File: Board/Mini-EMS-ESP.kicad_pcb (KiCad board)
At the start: 4 copper layers, 57.8 x 39 mm, 66 parts, among them J8 EMS, Q1 BC858, Q11 BC848, Q2 UMH3N, U1 ESP32-WROOM-32, U2 LM393, U3 MP1584, U4 CH340C, U5 USBLC6

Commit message: Minor fixes
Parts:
- C11: value 22u -> 47u
- R13, R15, R16: value 10K -> 100K
- R21: value 470 -> 220
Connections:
- net Net-(U3-EN) renamed /EMS interface/BUCK_EN
- net Net-(U3-FREQ) renamed /EMS interface/BUCK_FREQ
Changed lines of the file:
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@@
 	(net 28 "Net-(R10-Pad1)")
 	(net 29 "RX")
-	(net 30 "Net-(U3-FREQ)")
-	(net 31 "Net-(U3-EN)")
+	(net 30 "/EMS interface/BUCK_FREQ")
+	(net 31 "/EMS interface/BUCK_EN")
 	(net 32 "/EMS interface/BUCK_FB")
 	(net 33 "/CC2")
@@
 			)
 		)
-		(property "Value" "10K"
+		(property "Value" "100K"
 			(at 0 1.65 90)
 			(layer "F.Fab")
@@
 			(layers "F.Cu" "F.Mask" "F.Paste")
 			(roundrect_rratio 0.243902)
-			(net 30 "Net-(U3-FREQ)")
+			(net 30 "/EMS interface/BUCK_FREQ")
 			(pintype "passive")
 		)
@@
 			)
 		)
-		(property "Value" "10K"
+		(property "Value" "100K"
 			(at 0 1.65 0)
 			(layer "F.Fab")
@@
 			(layers "F.Cu" "F.Mask" "F.Paste")
 			(roundrect_rratio 0.243902)
-			(net 31 "Net-(U3-EN)")
+			(net 31 "/EMS interface/BUCK_EN")
 			(pintype "passive")
 		)
@@
 			(layers "F.Cu" "F.Mask" "F.Paste")
 			(roundrect_rratio 0.25)
-			(net 31 "Net-(U3-EN)")
+			(net 31 "/EMS interface/BUCK_EN")
 			(pinfunction "EN")
 			(pintype "input")
@@
 			(layers "F.Cu" "F.Mask" "F.Paste")
 			(roundrect_rratio 0.25)
-			(net 30 "Net-(U3-FREQ)")
+			(net 30 "/EMS interface/BUCK_FREQ")
 			(pinfunction "FREQ")
 			(pintype "input")
@@
 			)
 		)
-		(property "Value" "10K"
+		(property "Value" "100K"
 			(at 0 1.65 0)
 			(layer "F.Fab")
@@
 			(layers "F.Cu" "F.Mask" "F.Paste")
 			(roundrect_rratio 0.243902)
-			(net 31 "Net-(U3-EN)")
+			(net 31 "/EMS interface/BUCK_EN")
 			(pintype "passive")
 		)
@@
 			)
 		)
-		(property "Value" "22u"
+		(property "Value" "47u"
 			(at 0 1.85 90)
 			(layer "F.Fab")
@@
 			)
 		)
-		(property "Value" "470"
+		(property "Value" "220"
 			(at 0 1.65 90)
 			(layer "F.Fab")

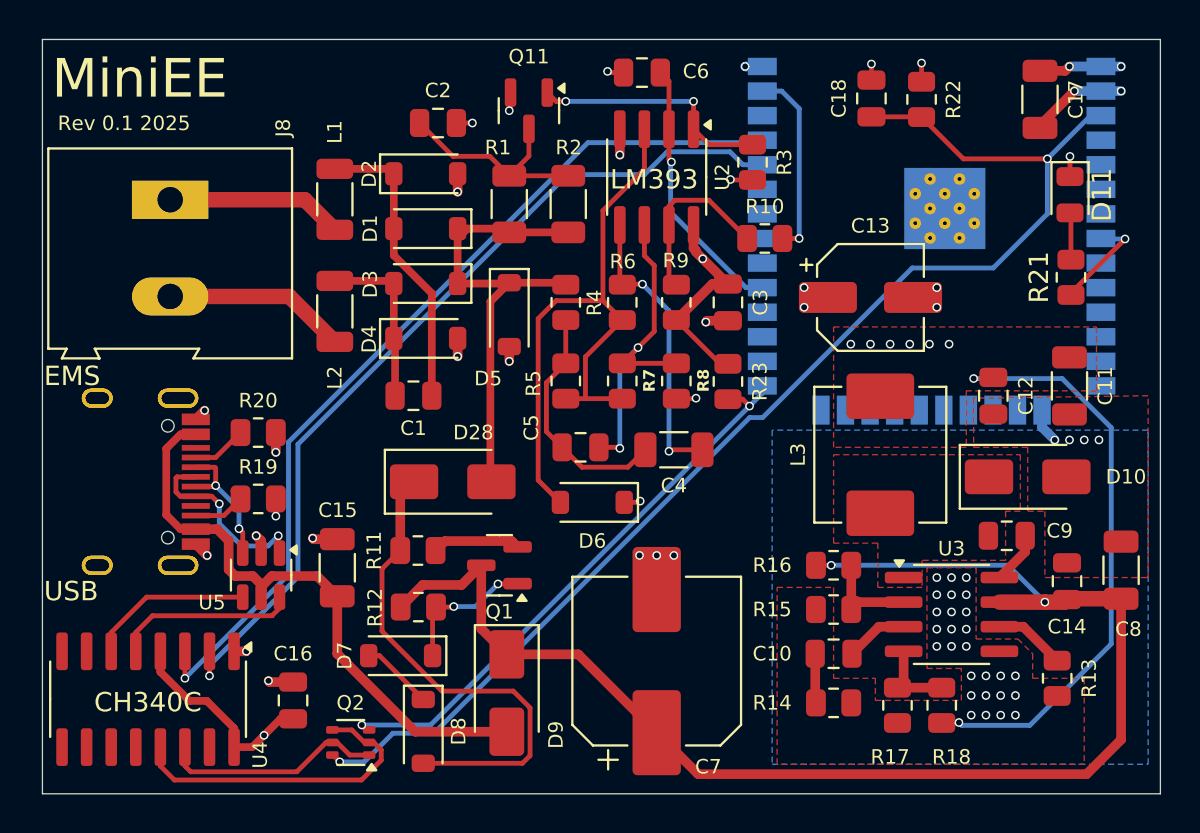
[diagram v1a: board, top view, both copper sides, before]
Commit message: Minor fixes and improvements. Changes board shape.
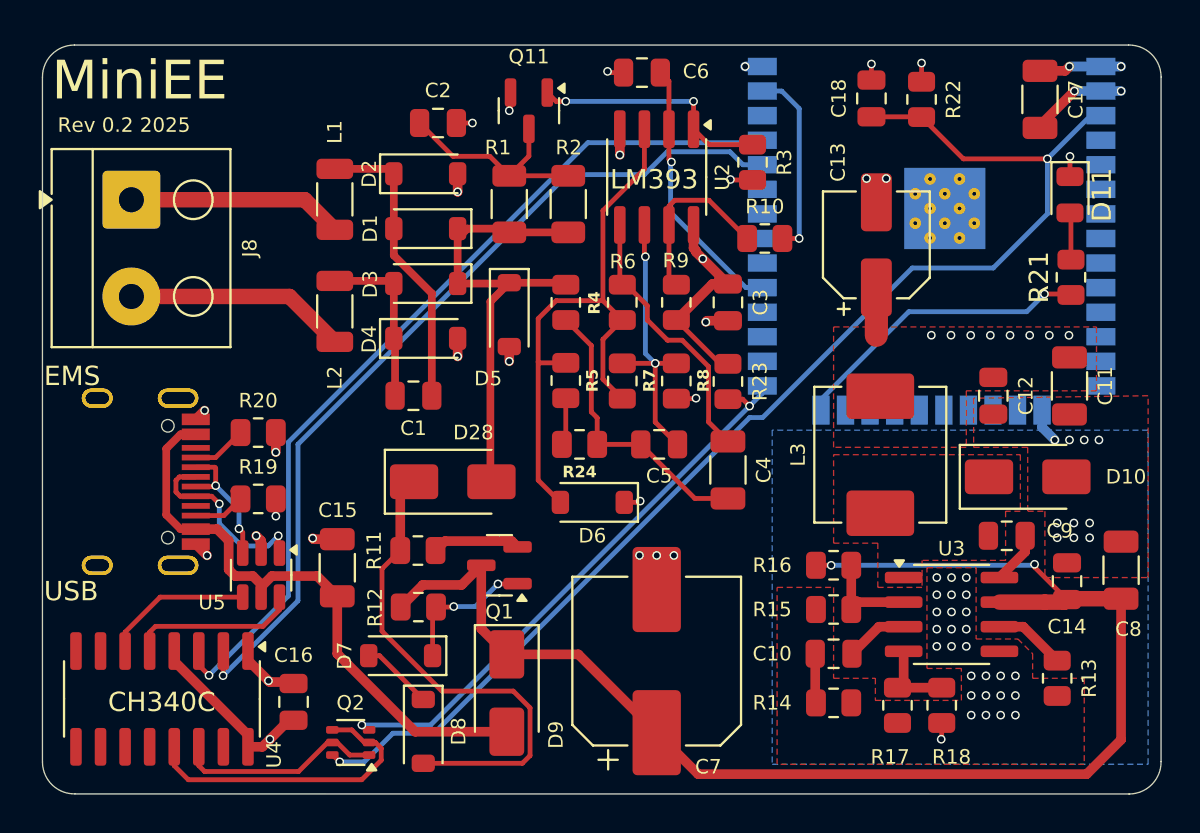
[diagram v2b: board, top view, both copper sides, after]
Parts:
- added R24: 33, Resistor_SMD:R_0805_2012Metric, F.Cu at (98.8, 106.8)
- C2: value 68p -> 1n5
- J8: footprint TerminalBlock:TerminalBlock_Altech_AK300-2_P5.00mm -> TerminalBlock_Altech:Altech_AK100_1x02_P5.00mm
- R11: value 15 -> 6R8
- R3, R9: value 3K3 -> 4K7
- R5: value 360 -> 330
- moved C5 4.07 mm to (102.9, 106.8)
- moved C4 2.98 mm to (106.4, 108.1), turned to -90 degrees
- moved C13 2.73 mm to (114.1, 96.5), turned to 90 degrees
- moved J8 2.01 mm to (75.6, 94.1)
- moved U4 0.72 mm to (77.2, 119.9)
- moved C16 0.08 mm to (84.0, 120.1)
- turned R5 to 90 degrees
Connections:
- net /EMS interface/EMS_POS renamed /EMS interface/U_EMS
- R21 pad 1: Net-(U1-IO32) -> Net-(U1-IO2)
- R5 pad 1: Net-(C4-Pad2) -> Net-(R24-Pad2)
- U1 pad 24: unconnected-(U1-IO2-Pad24) -> Net-(U1-IO2)
- U1 pad 8: Net-(U1-IO32) -> unconnected-(U1-IO32-Pad8)
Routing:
- net VDD: track 58.6 -> 30.8 mm, vias 16 -> 15
- net Net-(U1-IO2): track 0.00 -> 15.7 mm, vias 0 -> 1
- net Net-(U1-IO32): track 5.31 -> 0.00 mm, vias 1 -> 0
- net Net-(U2B--): track 17.5 -> 14.8 mm
- net Net-(C4-Pad2): track 12.4 -> 15.0 mm
- net Net-(R24-Pad2): track 0.00 -> 2.47 mm
- net Net-(J8-Pin_2): track 9.48 -> 11.5 mm
- net Net-(J8-Pin_1): track 9.15 -> 11.2 mm
- net /EMS interface/EMS_UREF: track 32.6 -> 31.2 mm
- net GND: track 26.1 -> 27.5 mm, vias 59 -> 64
- net /EMS interface/BUCK_VIN: track 71.5 -> 72.8 mm
- net Net-(U2B-+): track 15.2 -> 14.1 mm, vias 2 -> 0
- net Net-(Q2A-E1): track 11.5 -> 10.8 mm
- net /UD-: track 8.53 -> 7.81 mm
- net Net-(Q2A-B1): track 16.6 -> 15.9 mm
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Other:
- board size 57.8 x 39 mm -> 57.8 x 38.7 mm
- board text added: "Rev 0.2 2025"
- board text removed: "Rev 0.1 2025"

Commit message: Fixes constant current circuit.
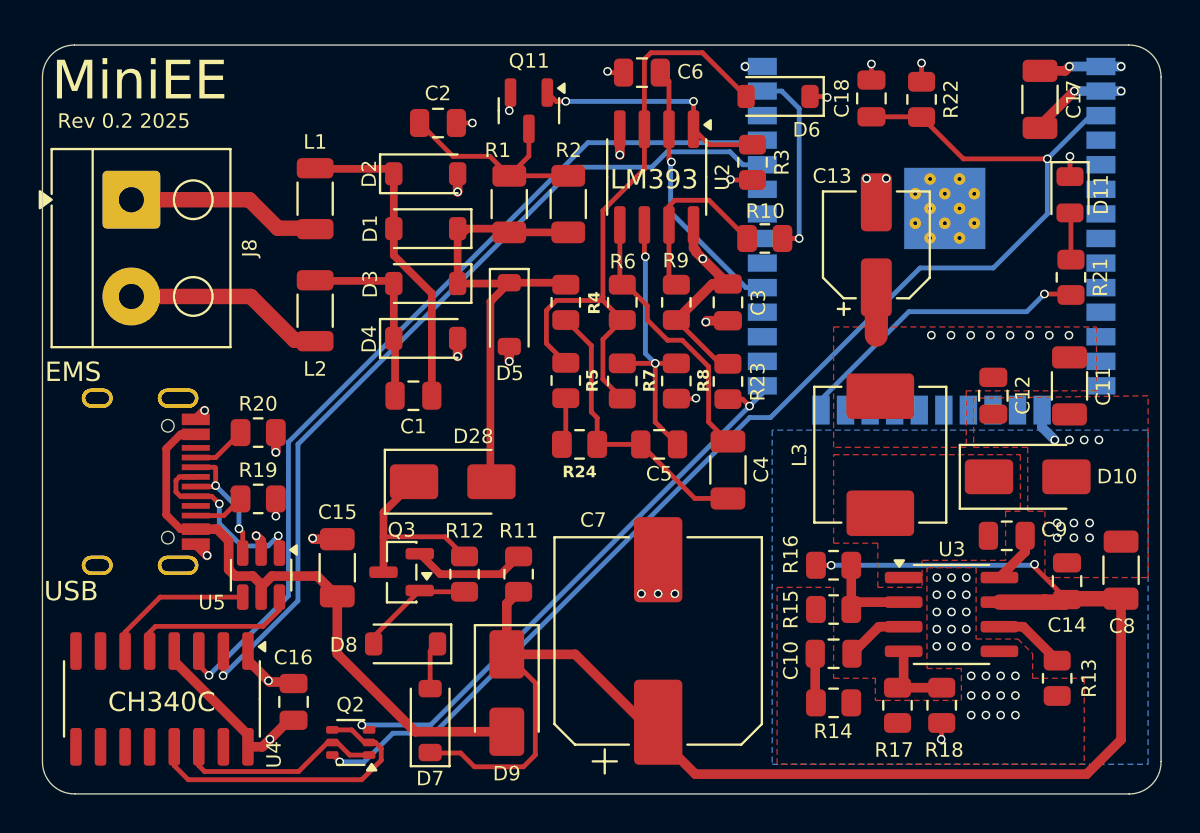
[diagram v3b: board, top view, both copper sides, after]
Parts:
- removed Q1: BC858, Package_TO_SOT_SMD:SOT-23
- added Q3: BC848, Package_TO_SOT_SMD:SOT-23, F.Cu at (89.6, 113.4)
- C7: value 330u -> 1000u; footprint Capacitor_SMD:CP_Elec_8x10.5 -> Capacitor_SMD:CP_Elec_10x10.5
- R11: value 6R8 -> 5.6
- R12: value 10K -> 2K2
- R21: value 220 -> 330
- moved D6 23.1 mm to (109.0, 88.8)
- moved R11 5.35 mm to (95.6, 113.5), turned to 90 degrees
- moved D8 4.61 mm to (89.8, 117.1), turned to 180 degrees
- moved D7 3.68 mm to (91.0, 121.1), turned to 90 degrees
- moved R12 2.93 mm to (92.8, 113.5), turned to 90 degrees
- moved C7 1.04 mm to (102.8, 116.9)
- moved L1 1.02 mm to (85.1, 94.1)
- moved L2 1.02 mm to (85.1, 99.9)
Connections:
- D7 pad 1: Net-(D7-K) -> /EMS interface/BUCK_VIN
- D8 pad 2: Net-(D28-K) -> Net-(D8-A)
- R11 pad 1: Net-(Q1-E) -> /EMS interface/BUCK_VIN
- R11 pad 2: Net-(D28-K) -> Net-(Q3-E)
- R12 pad 1: /EMS interface/BUCK_VIN -> Net-(D8-A)
- R12 pad 2: Net-(D7-K) -> Net-(D28-K)
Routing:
- net Net-(D28-K): track 25.9 -> 9.94 mm
- net Net-(D7-K): track 7.30 -> 0.00 mm, vias 2 -> 0
- net Net-(D8-A): track 0.00 -> 6.09 mm
- net Net-(Q3-E): track 0.00 -> 5.92 mm
- net /EMS interface/BUCK_VIN: track 72.8 -> 78.3 mm
- net Net-(Q1-E): track 4.57 -> 0.00 mm
- net Net-(D7-A): track 3.76 -> 2.47 mm
- net /EMS interface/EMS_UREF: track 31.2 -> 32.3 mm
- net Net-(J8-Pin_2): track 11.5 -> 10.5 mm
- net Net-(J8-Pin_1): track 11.2 -> 10.1 mm
- net Net-(D3-A): track 8.93 -> 9.96 mm
- net Net-(D1-A): track 15.4 -> 16.5 mm

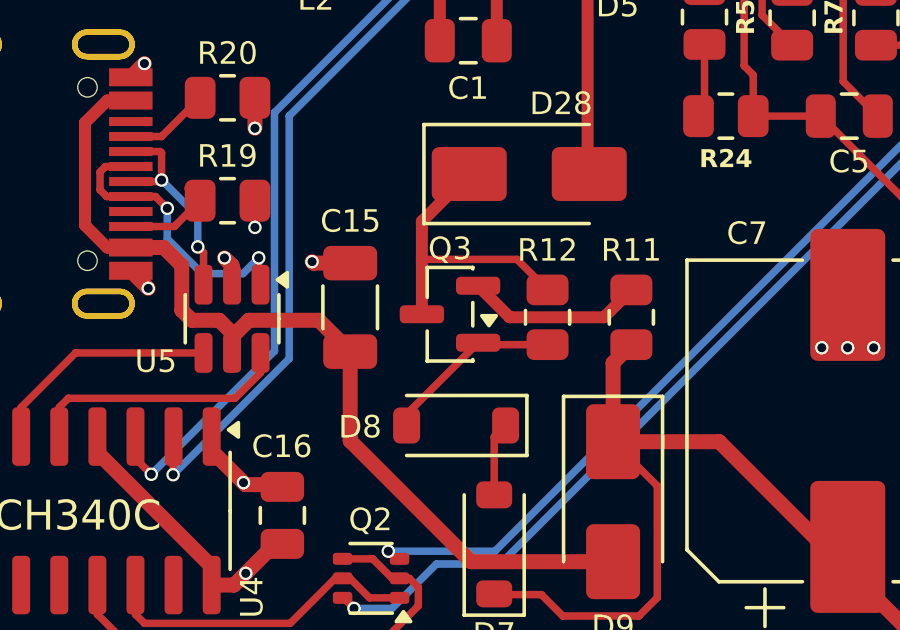
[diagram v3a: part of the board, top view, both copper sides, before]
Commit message: Replaces Q3 with higher current type
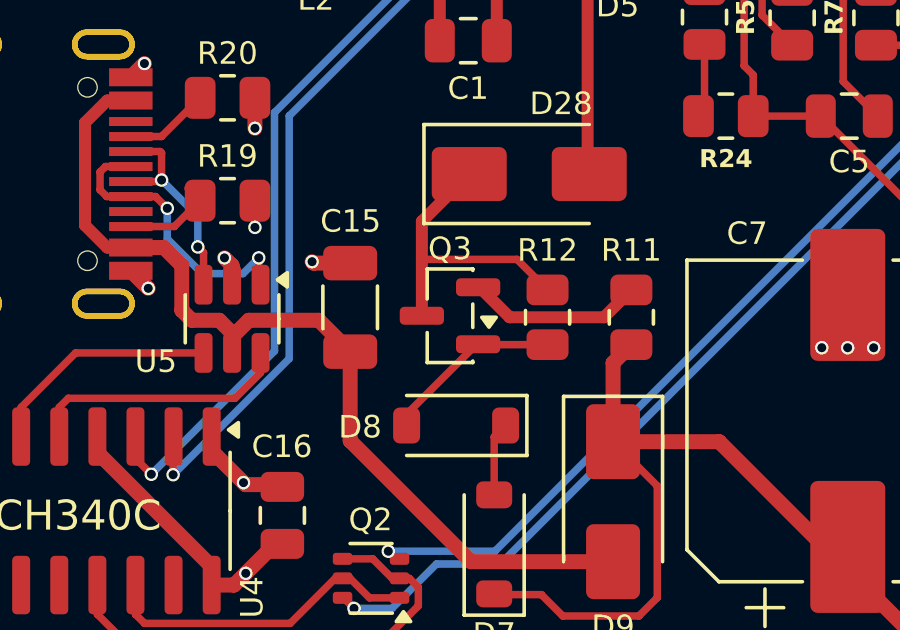
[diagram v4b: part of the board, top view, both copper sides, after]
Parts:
- Q3: value BC848 -> MMBT3904
- moved Q3 0.05 mm to (89.6, 113.4)
